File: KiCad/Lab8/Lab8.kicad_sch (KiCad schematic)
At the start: 22 parts, among them M1 Motor, M2 Motor, SW1 Reset, U1 PIC32MX170F256B, U2 SN754410NE

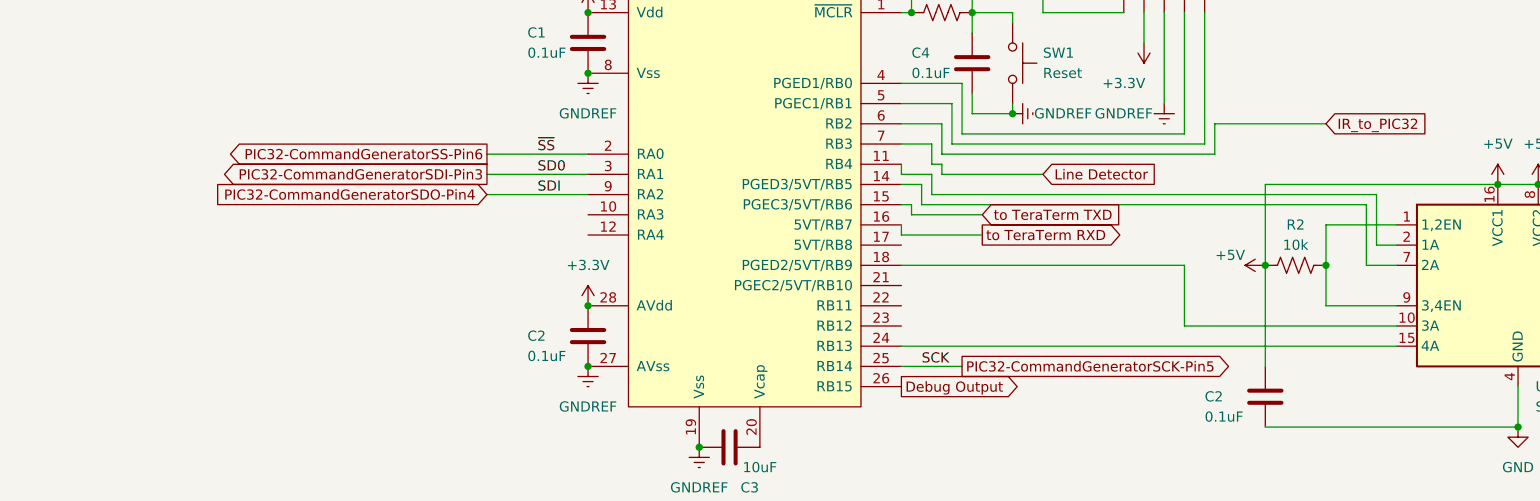
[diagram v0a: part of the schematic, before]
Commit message: wire connect and IR detect and SPI and state machine test pass
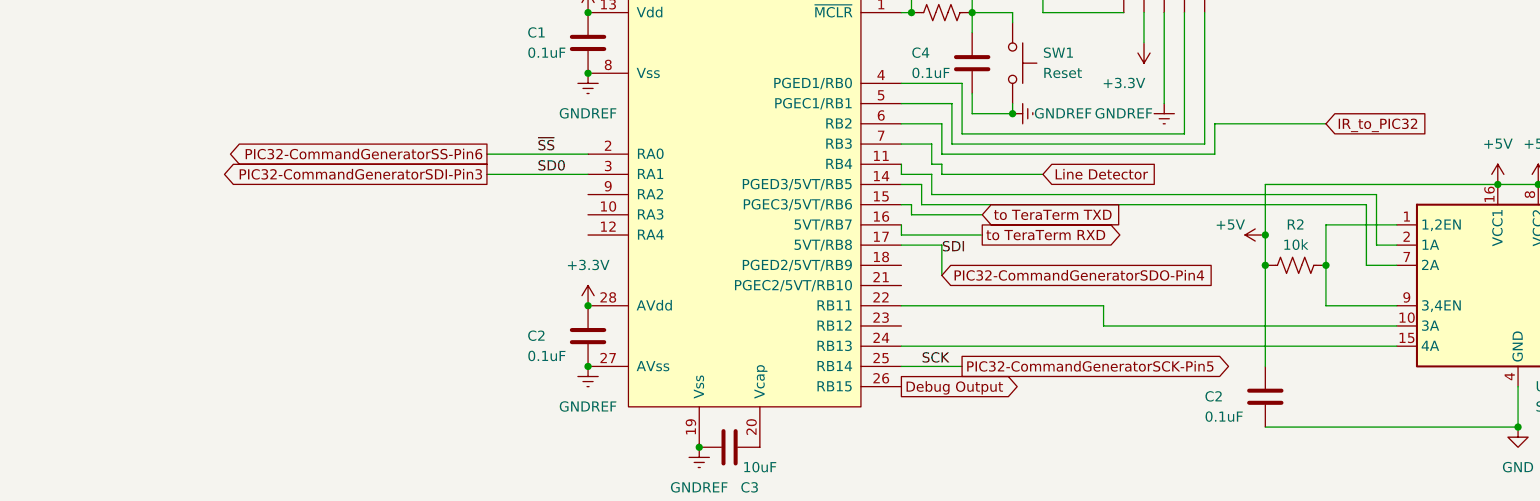
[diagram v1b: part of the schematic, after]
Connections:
- net PIC32-CommandGeneratorSDO-Pin4: now also U1.17 (5VT/RB8); no longer U1.9 (RA2)
- net at U1.18 (PGED2/5VT/RB9): no longer U2.10 (3A)
- net at U1.22 (RB11): now also U2.10 (3A)
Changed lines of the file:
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@@
   (junction (at 184.15 76.2) (diameter 0) (color 0 0 0 0)
   )
+  (junction (at 176.53 72.39) (diameter 0) (color 0 0 0 0)
+  )
   (junction (at 144.78 57.15) (diameter 0) (color 0 0 0 0)
   )
@@
     (stroke (width 0) (type default))
   )
+  (wire (pts (xy 156.21 83.82) (xy 156.21 81.28))
+    (stroke (width 0) (type default))
+  )
   (wire (pts (xy 134.62 67.31) (xy 190.5 67.31))
     (stroke (width 0) (type default))
@@
     (stroke (width 0) (type default))
   )
-  (wire (pts (xy 166.37 83.82) (xy 193.04 83.82))
+  (wire (pts (xy 156.21 83.82) (xy 193.04 83.82))
     (stroke (width 0) (type default))
   )
@@
     (stroke (width 0) (type default))
   )
+  (wire (pts (xy 156.21 81.28) (xy 130.81 81.28))
+    (stroke (width 0) (type default))
+  )
   (wire (pts (xy 236.22 58.42) (xy 236.22 68.58))
     (stroke (width 0) (type default))
@@
     (stroke (width 0) (type default))
   )
-  (wire (pts (xy 91.44 67.31) (xy 78.74 67.31))
-    (stroke (width 0) (type default))
-  )
   (wire (pts (xy 236.22 68.58) (xy 271.78 68.58))
     (stroke (width 0) (type default))
@@
     (stroke (width 0) (type default))
   )
-  (wire (pts (xy 166.37 76.2) (xy 166.37 83.82))
-    (stroke (width 0) (type default))
-  )
   (wire (pts (xy 265.43 81.28) (xy 265.43 88.9))
     (stroke (width 0) (type default))
@@
     (stroke (width 0) (type default))
   )
+  (wire (pts (xy 135.89 73.66) (xy 135.89 77.47))
+    (stroke (width 0) (type default))
+  )
   (wire (pts (xy 134.62 60.96) (xy 134.62 63.5))
     (stroke (width 0) (type default))
@@
     (stroke (width 0) (type default))
   )
+  (wire (pts (xy 130.81 73.66) (xy 135.89 73.66))
+    (stroke (width 0) (type default))
+  )
   (wire (pts (xy 130.81 58.42) (xy 135.89 58.42))
     (stroke (width 0) (type default))
@@
     (stroke (width 0) (type default))
   )
-  (wire (pts (xy 130.81 76.2) (xy 166.37 76.2))
-    (stroke (width 0) (type default))
-  )
   (wire (pts (xy 193.04 81.28) (xy 184.15 81.28))
     (stroke (width 0) (type default))
@@
     (stroke (width 0) (type default))
   )
+  (wire (pts (xy 176.53 72.39) (xy 176.53 76.2))
+    (stroke (width 0) (type default))
+  )
   (wire (pts (xy 140.97 72.39) (xy 130.81 72.39))
     (stroke (width 0) (type default))
@@
     (stroke (width 0) (type default))
   )
-  (wire (pts (xy 176.53 66.04) (xy 176.53 76.2))
+  (wire (pts (xy 176.53 66.04) (xy 176.53 72.39))
     (stroke (width 0) (type default))
   )
@@
     (stroke (width 0) (type default))
   )
-  (label "SDI" (at 85.09 67.31 0) (fields_autoplaced)
+  (label "SDI" (at 135.89 74.93 0) (fields_autoplaced)
     (effects (font (size 1.27 1.27)) (justify left bottom))
   )
@@
     (effects (font (size 1.27 1.27)) (justify left bottom))
   )
-  (global_label "PIC32-CommandGeneratorSDO-Pin4" (shape input) (at 78.74 67.31 180) (fields_autoplaced)
-    (effects (font (size 1.27 1.27)) (justify right))
-    (property "Intersheetrefs" "${INTERSHEET_REFS}" (at 40.558 67.31 0)
-      (effects (font (size 1.27 1.27)) (justify right) hide)
+  (global_label "PIC32-CommandGeneratorSDO-Pin4" (shape input) (at 135.89 77.47 0) (fields_autoplaced)
+    (effects (font (size 1.27 1.27)) (justify left))
+    (property "Intersheetrefs" "${INTERSHEET_REFS}" (at 174.072 77.47 0)
+      (effects (font (size 1.27 1.27)) (justify left) hide)
     )
   )
@@
     )
   )
-  (symbol (lib_id "power:+5V") (at 176.53 76.2 90) (unit 1)
+  (symbol (lib_id "power:+5V") (at 176.53 72.39 90) (unit 1)
     (in_bom yes) (on_board yes) (dnp no)
-    (property "Reference" "#PWR012" (at 180.34 76.2 0)
-      (effects (font (size 1.27 1.27)) hide)
-    )
-    (property "Value" "+5V" (at 173.99 74.93 90)
-      (effects (font (size 1.27 1.27)) (justify left))
-    )
-    (property "Footprint" "" (at 176.53 76.2 0)
-      (effects (font (size 1.27 1.27)) hide)
-    )
-    (property "Datasheet" "" (at 176.53 76.2 0)
-      (effects (font (size 1.27 1.27)) hide)
-    )
+    (property "Reference" "#PWR012" (at 180.34 72.39 0)
+      (effects (font (size 1.27 1.27)) hide)
+    )
+    (property "Value" "+5V" (at 173.99 71.12 90)
+      (effects (font (size 1.27 1.27)) (justify left))
+    )
+    (property "Footprint" "" (at 176.53 72.39 0)
+      (effects (font (size 1.27 1.27)) hide)
+    )
+    (property "Datasheet" "" (at 176.53 72.39 0)
+      (effects (font (size 1.27 1.27)) hide)
+    )
